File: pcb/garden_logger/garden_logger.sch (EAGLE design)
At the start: 2 parts

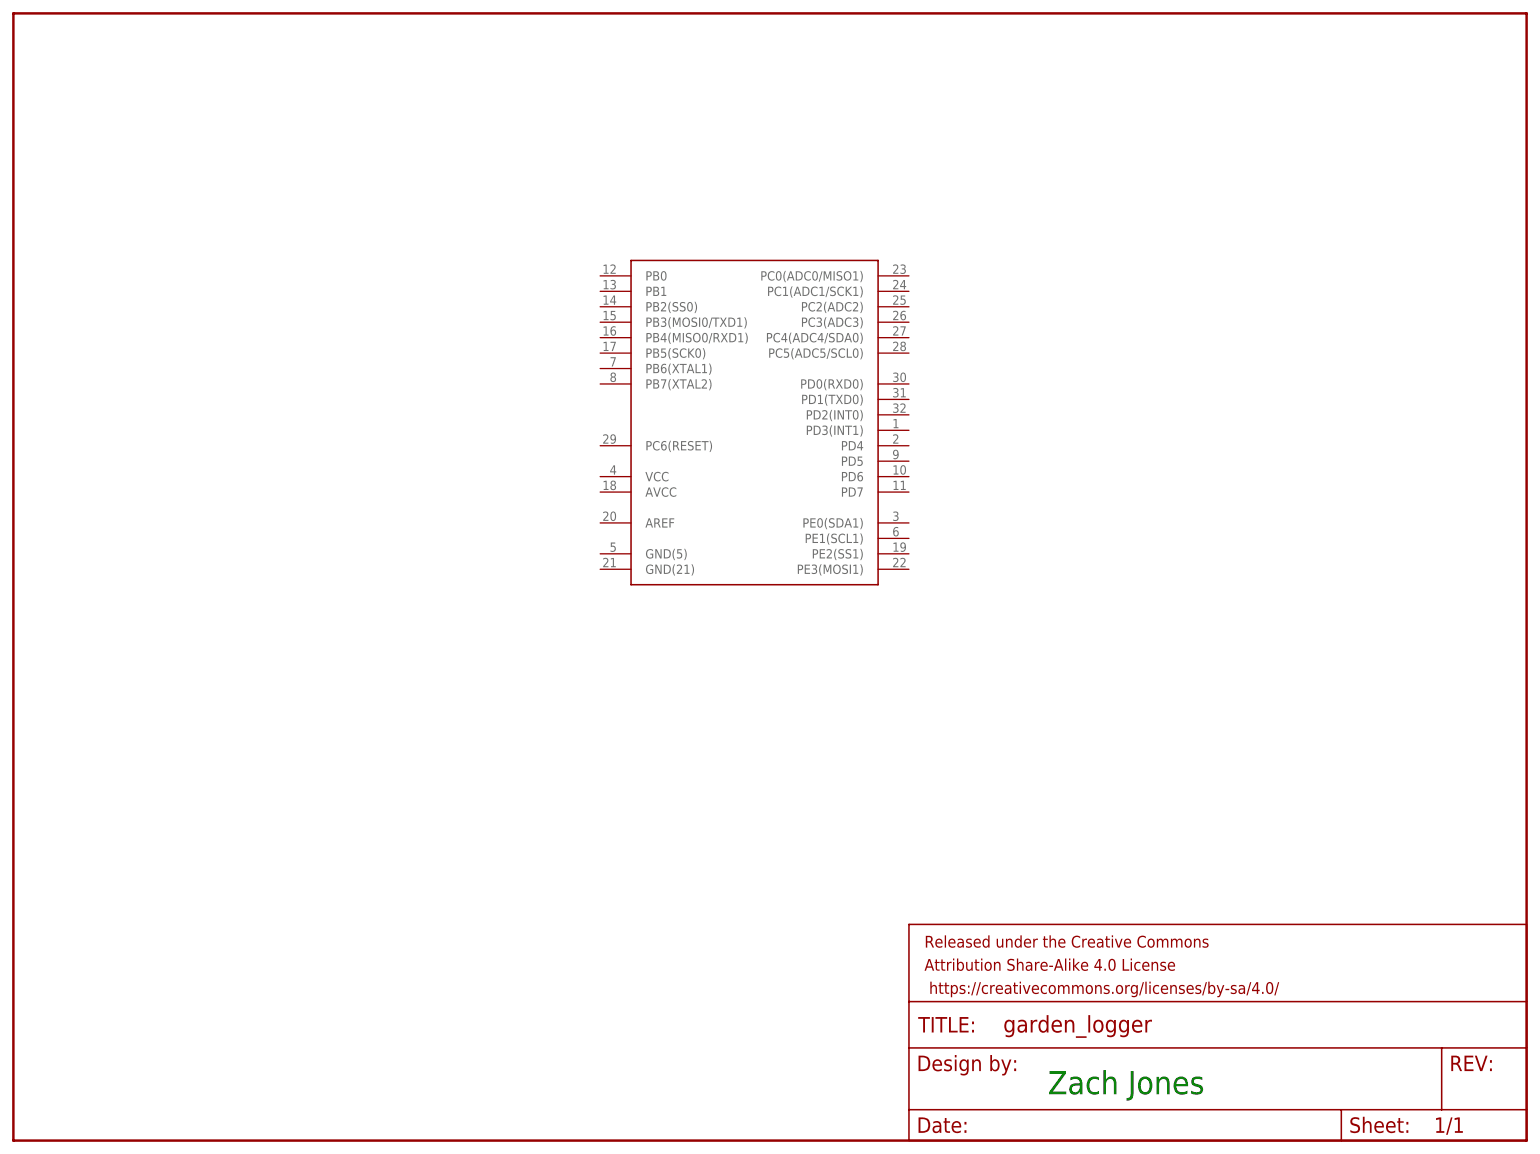
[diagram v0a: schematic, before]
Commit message: basic support circuit and breakout pin headers
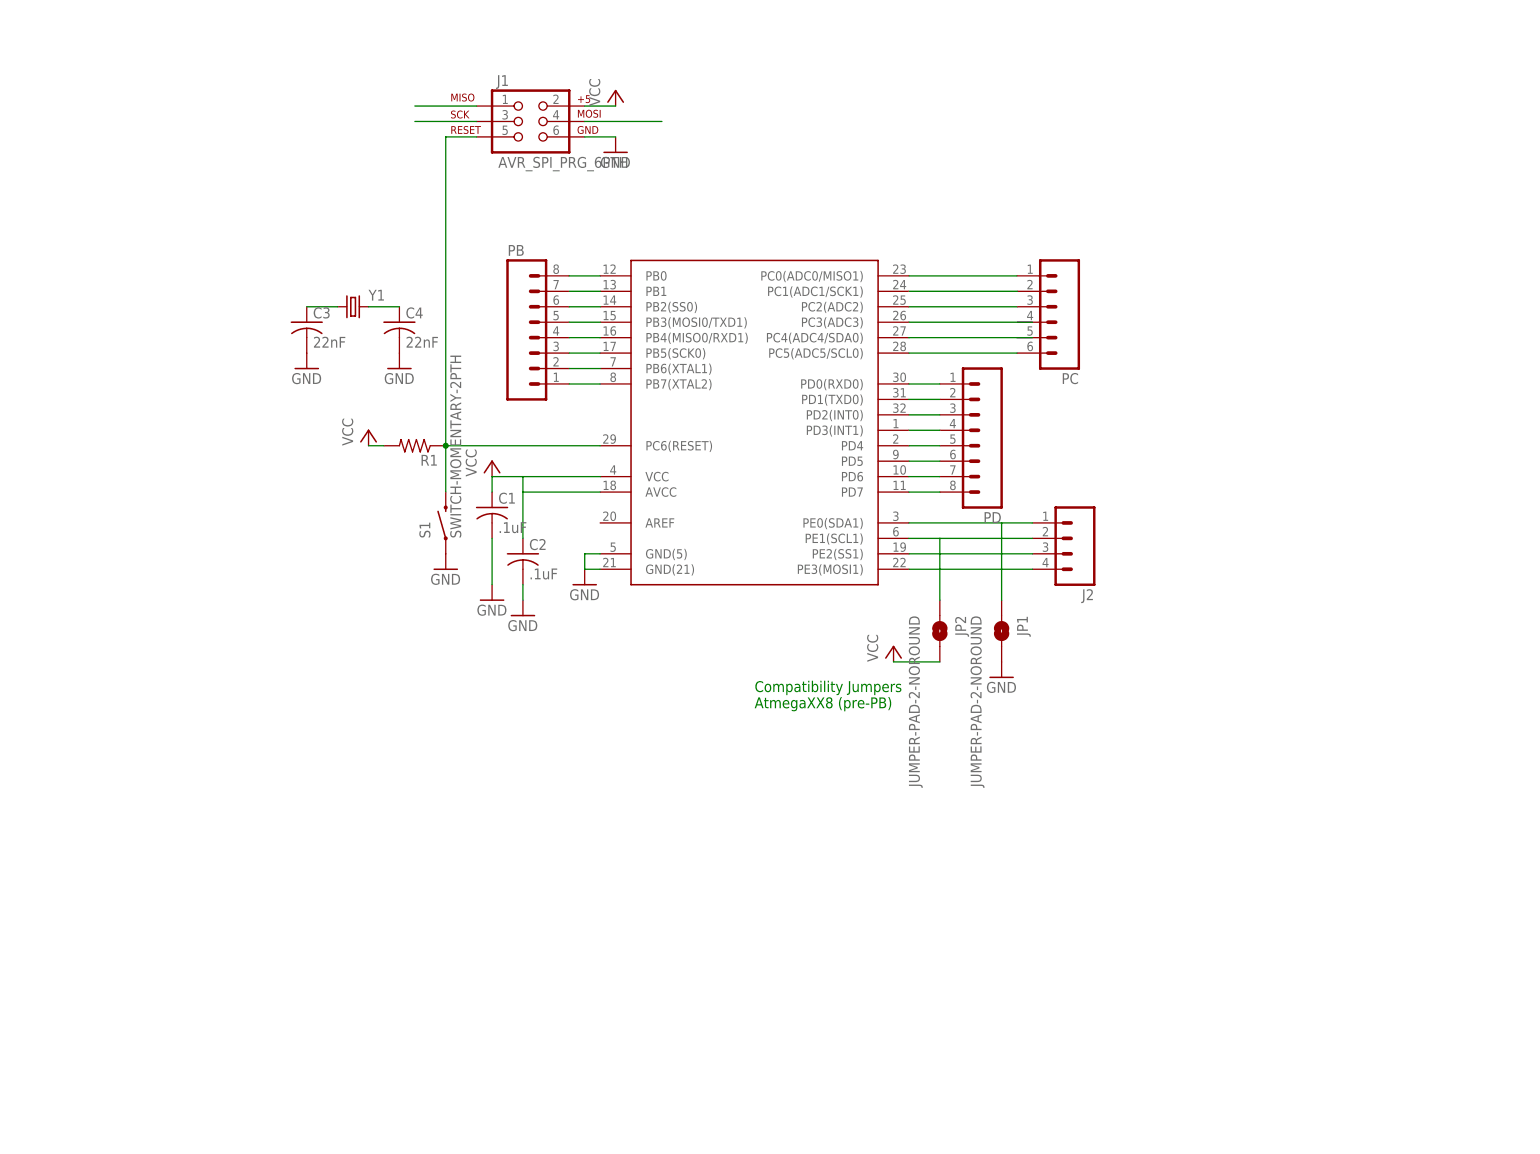
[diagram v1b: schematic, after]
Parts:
- removed FRAME1: FRAME-LETTER, SparkFun-Aesthetics:FRAME-LETTER
- added C1, C2: .1uF, rcl:C-USC0805
- added C3, C4: 22nF, rcl:C-USC0805
- added J1: AVR_SPI_PRG_6PTH, SparkFun-Connectors:AVR_SPI_PRG_6PTH
- added J2: (no value), SparkFun-Connectors:M04PTH
- added JP1, JP2: JUMPER-PAD-2-NOROUND, SparkFun-Passives:JUMPER-PAD-2-NOROUND
- added PB, PD: (no value), SparkFun-Connectors:M08
- added PC: (no value), SparkFun-Connectors:M06SILK_FEMALE_PTH
- added R1: (no value), rcl:R-US_R0805
- added S1: SWITCH-MOMENTARY-2PTH, SparkFun-Electromechanical:SWITCH-MOMENTARY-2PTH
- added Y1: (no value), SparkFun-FreqCtrl:CRYSTALHC49US
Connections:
- new net GND: C1.2, C2.2, C3.2, C4.2, J1.6, JP1.2, S1.1, U$1.GND(21), U$1.GND(5)
- new net N$1: J1.5, R1.1, S1.2, U$1.PC6(RESET)
- new net PIN1: PD.4, U$1.PD3(INT1)
- new net PIN10: PD.7, U$1.PD6
- new net PIN11: PD.8, U$1.PD7
- new net PIN12: PB.8, U$1.PB0
- new net PIN13: PB.7, U$1.PB1
- new net PIN14: PB.6, U$1.PB2(SS0)
- new net PIN15: J1.4, PB.5, U$1.PB3(MOSI0/TXD1)
- new net PIN16: J1.1, PB.4, U$1.PB4(MISO0/RXD1)
- new net PIN17: J1.3, PB.3, U$1.PB5(SCK0)
- new net PIN19: J2.3, U$1.PE2(SS1)
- new net PIN2: PD.5, U$1.PD4
- new net PIN22: J2.4, U$1.PE3(MOSI1)
- new net PIN23: PC.1, U$1.PC0(ADC0/MISO1)
- new net PIN24: PC.2, U$1.PC1(ADC1/SCK1)
- new net PIN25: PC.3, U$1.PC2(ADC2)
- new net PIN26: U$1.PC3(ADC3)
- new net PIN27: U$1.PC4(ADC4/SDA0)
- new net PIN28: PC.6, U$1.PC5(ADC5/SCL0)
- new net PIN3: J2.1, JP1.1, U$1.PE0(SDA1)
- new net PIN30: PD.1, U$1.PD0(RXD0)
- new net PIN31: PD.2, U$1.PD1(TXD0)
- new net PIN32: PD.3, U$1.PD2(INT0)
- new net PIN6: J2.2, JP2.1, U$1.PE1(SCL1)
- new net PIN7: C3.1, PB.2, U$1.PB6(XTAL1), Y1.1
- new net PIN8: C4.1, PB.1, U$1.PB7(XTAL2), Y1.2
- new net PIN9: PD.6, U$1.PD5
- new net VCC: C1.1, C2.1, J1.2, JP2.2, R1.2, U$1.AVCC, U$1.VCC
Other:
- note added: "Compatibility Jumpers AtmegaXX8 (pre-PB)"
- note removed: "Zach Jones"

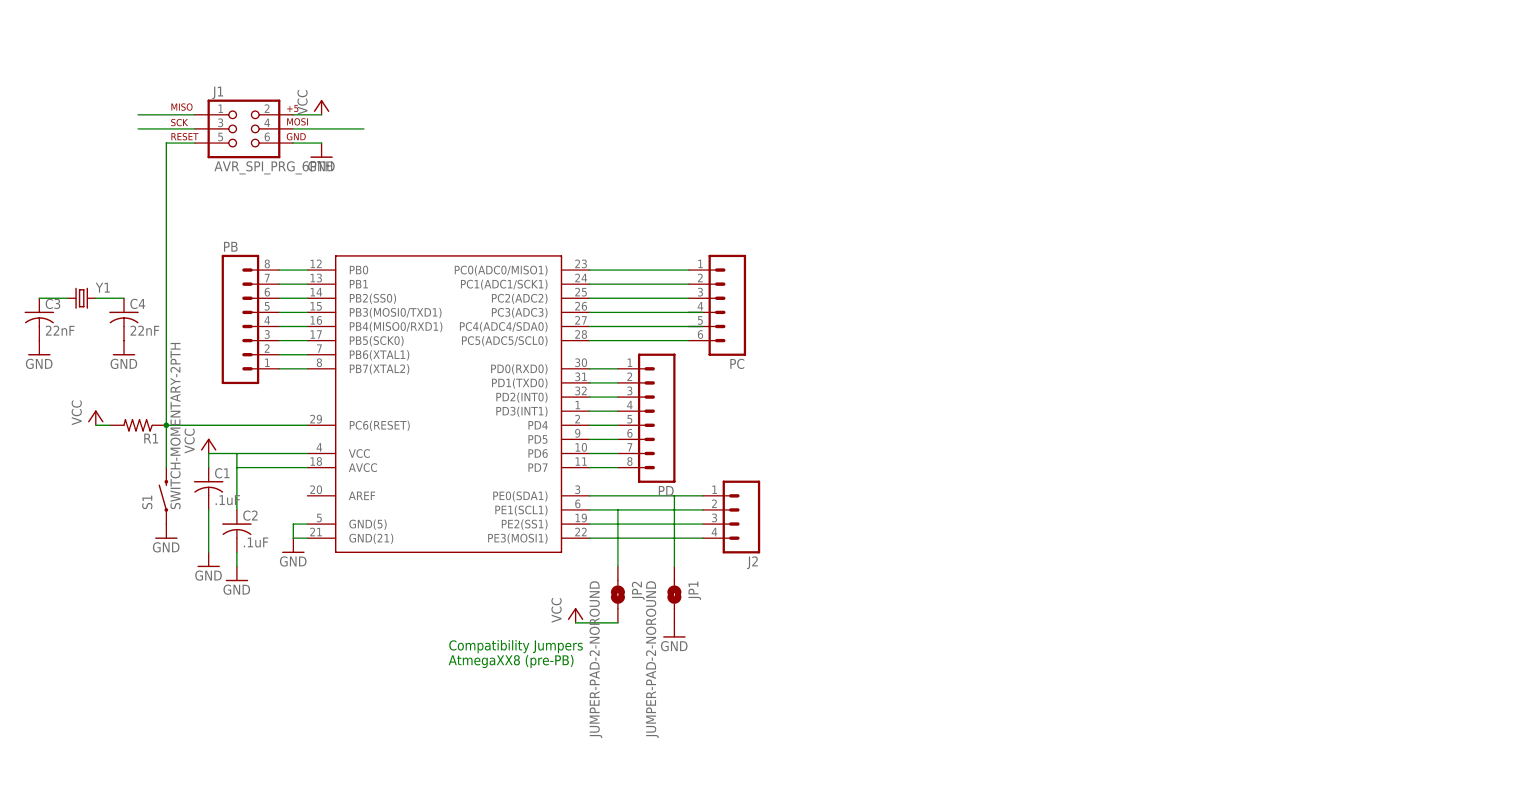
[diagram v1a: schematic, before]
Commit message: added some extra breakouts
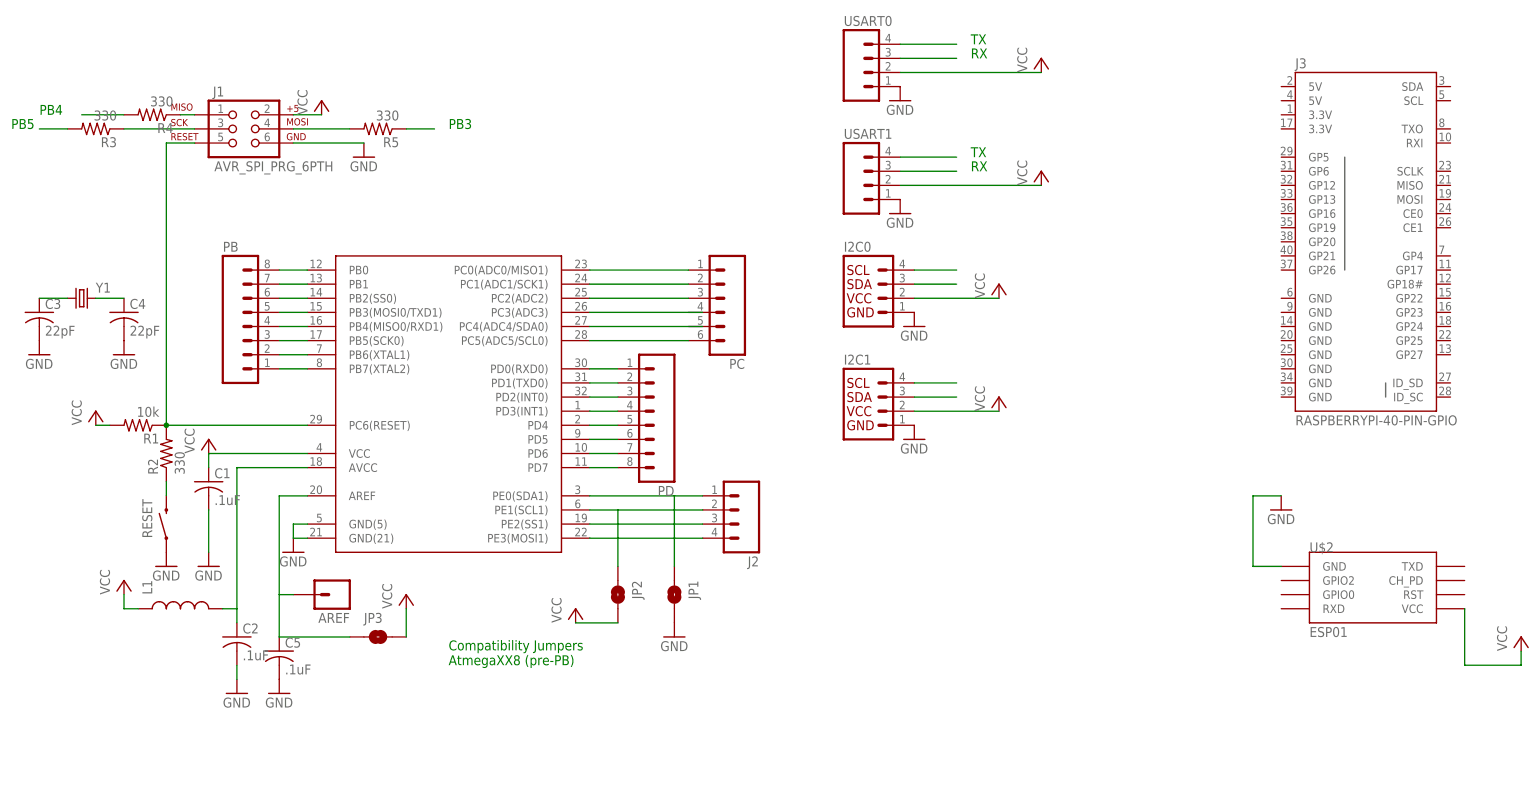
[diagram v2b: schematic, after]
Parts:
- removed S1: SWITCH-MOMENTARY-2PTH, SparkFun-Electromechanical:SWITCH-MOMENTARY-2PTH
- added AREF: (no value), SparkFun-Connectors:M01PTH
- added C5: .1uF, rcl:C-USC0805
- added I2C0, I2C1: (no value), SparkFun-Connectors:I2C_STANDARD
- added J3: RASPBERRYPI-40-PIN-GPIO, SparkFun-Boards:RASPBERRYPI-40-PIN-GPIO
- added JP3: JUMPER-PAD-2-NOROUND, SparkFun-Passives:JUMPER-PAD-2-NOROUND
- added L1: (no value), SparkFun-Passives:INDUCTOR0805
- added R2, R3, R4, R5: 330, rcl:R-US_R0805
- added RESET: SWITCH-MOMENTARY-2PTH, SparkFun-Electromechanical:SWITCH-MOMENTARY-2PTH
- added U$2: ESP01, esp8266modules:ESP01
- added USART0, USART1: (no value), SparkFun-Connectors:M04PTH
- C3, C4: value 22nF -> 22pF
- R1: value (none) -> 10k
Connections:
- net PIN1 renamed PD3
- net PIN10 renamed PD6
- net PIN11 renamed PD7
- net PIN12 renamed PB0
- net PIN13 renamed PB1
- net PIN14 renamed PB2
- net PIN19 renamed PE2
- net PIN2 renamed PD4
- net PIN22 renamed PE3
- net PIN23 renamed PC0
- net PIN24 renamed PC1
- net PIN25 renamed PC2
- net PIN26 renamed PC3
- net PIN32 renamed PD2
- net PIN7 renamed PB6
- net PIN8 renamed PB7
- net PIN9 renamed PD5
- removed net PIN15: J1.4, PB.5, U$1.PB3(MOSI0/TXD1)
- removed net PIN16: J1.1, PB.4, U$1.PB4(MISO0/RXD1)
- removed net PIN17: J1.3, PB.3, U$1.PB5(SCK0)
- removed net PIN27: U$1.PC4(ADC4/SDA0)
- removed net PIN28: PC.6, U$1.PC5(ADC5/SCL0)
- removed net PIN3: J2.1, JP1.1, U$1.PE0(SDA1)
- removed net PIN30: PD.1, U$1.PD0(RXD0)
- removed net PIN31: PD.2, U$1.PD1(TXD0)
- removed net PIN6: J2.2, JP2.1, U$1.PE1(SCL1)
- new net AVCC: C2.1, L1.2, U$1.AVCC
- new net N$2: R2.1, RESET.2
- new net N$3: J1.1, R4.1
- new net N$4: J1.3, R3.1
- new net N$5: J1.4, R5.2
- new net PB3: PB.5, R5.1, U$1.PB3(MOSI0/TXD1), USART1.3, USART1.4
- new net PB4: PB.4, R4.2, U$1.PB4(MISO0/RXD1)
- new net PB5: PB.3, R3.2, U$1.PB5(SCK0)
- new net PC4: I2C0.3, U$1.PC4(ADC4/SDA0)
- new net PC5: I2C0.4, PC.6, U$1.PC5(ADC5/SCL0)
- new net PC6: J1.5, R1.1, R2.2, U$1.PC6(RESET)
- new net PD0: PD.1, U$1.PD0(RXD0), USART0.3
- new net PD1: PD.2, U$1.PD1(TXD0), USART0.4
- new net PE0: I2C1.3, J2.1, JP1.1, U$1.PE0(SDA1)
- new net PE1: I2C1.4, J2.2, JP2.1, U$1.PE1(SCL1)
- net GND: now also C5.2, I2C0.1, I2C1.1, RESET.1, U$2.GND, USART0.1, USART1.1; no longer S1.1
- net N$1: now also AREF.1, C5.1, JP3.1, U$1.AREF; no longer J1.5, R1.1, S1.2, U$1.PC6(RESET)
- net VCC: now also I2C0.2, I2C1.2, JP3.2, L1.1, U$2.VCC, USART0.2, USART1.2; no longer C2.1, U$1.AVCC
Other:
- note added: "PB3"
- note added: "PB4"
- note added: "PB5"
- note added: "RX"
- note added: "TX"
- moved on the sheet: C2

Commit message: most avr stuff connected.  working on rpi breakout section.  added emtpy board layout
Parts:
- added H1, H2, H3, H4: STAND-OFF, SparkFun-Electromechanical:STAND-OFF
- added J4: (no value), SparkFun-Connectors:M02PTH
- added JP4, JP5: JUMPER-PAD-2-NOROUND, SparkFun-Passives:JUMPER-PAD-2-NOROUND
- added L2: 10uH, SparkFun-Passives:INDUCTOR0805
- added LOGO1: OSHW-LOGOS, SparkFun-Aesthetics:OSHW-LOGOS
- added RPI-I2C: (no value), SparkFun-Connectors:I2C_STANDARD
- added RPI-USART: (no value), SparkFun-Connectors:M04PTH
- L1: value (none) -> 10uH
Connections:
- new net AVRVCC: C1.1, L2.2, U$1.VCC
- new net N$12: J3.SCL, RPI-I2C.4
- new net N$13: J3.SDA, RPI-I2C.3
- new net N$6: J4.1, JP5.2, U$2.CH_PD
- new net N$7: J4.2, JP4.1, U$2.RST
- new net N$8: J3.TXO, RPI-USART.4
- new net N$9: J3.RXI, RPI-USART.3
- net GND: now also J3.GND@14, J3.GND@20, J3.GND@25, J3.GND@30, J3.GND@34, J3.GND@39, J3.GND@6, J3.GND@9, RPI-I2C.1, RPI-USART.1
- net PD0: now also U$2.TXD
- net PD1: now also U$2.RXD
- net PD6: now also JP5.1
- net PD7: now also JP4.2
- net VCC: now also L2.1, RPI-I2C.2, RPI-USART.2; no longer C1.1, U$1.VCC
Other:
- note added: "Jumpering over inductor pads if not including inductors"
- note added: "PD0"
- note added: "PD1"
- moved on the sheet: C1, C2, L1, RESET

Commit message: added buttons and leds.  started laying out board
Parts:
- added ADC: (no value), SparkFun-Connectors:M08
- added BUTTON, LED: (no value), SparkFun-Connectors:M03PTH
- added BUTTON1, BUTTON2, BUTTON3: SWITCH-MOMENTARY-2PTH, SparkFun-Electromechanical:SWITCH-MOMENTARY-2PTH
- added LED1, LED2, LED3: (no value), led:LEDCHIPLED_0805
- added R10, R11, R9: 10k, rcl:R-US_R0805
- added R6, R7, R8: 330, rcl:R-US_R0805
- renumbered J2 to PE, J4 to ESP-01
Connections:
- new net N$11: LED1.C, R6.2
- new net N$14: LED2.C, R7.2
- new net N$15: LED3.C, R8.2
- new net N$16: LED.1, LED1.A
- new net N$17: LED.2, LED2.A
- new net N$18: LED.3, LED3.A
- new net N$20: BUTTON.3, BUTTON3.2, R11.2
- new net N$21: BUTTON.2, BUTTON2.2, R10.2
- new net N$22: BUTTON.1, BUTTON1.2, R9.2
- net GND: now also BUTTON1.1, BUTTON2.1, BUTTON3.1, R6.1, R7.1, R8.1
- net PC0: now also ADC.1
- net PC1: now also ADC.2
- net PC2: now also ADC.3
- net PC3: now also ADC.4
- net PC4: now also ADC.5
- net PC5: now also ADC.6
- net PE2: now also ADC.7
- net PE3: now also ADC.8
- net VCC: now also R10.1, R11.1, R9.1

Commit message: removed rpi header to have bigger proto area.  Mostly done routeing
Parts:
- removed ADC: (no value), SparkFun-Connectors:M08
- removed ESP-01: (no value), SparkFun-Connectors:M02PTH
- removed J3: RASPBERRYPI-40-PIN-GPIO, SparkFun-Boards:RASPBERRYPI-40-PIN-GPIO
- removed JP1, JP2, JP3, JP4, JP5: JUMPER-PAD-2-NOROUND, SparkFun-Passives:JUMPER-PAD-2-NOROUND
- removed RPI-I2C: (no value), SparkFun-Connectors:I2C_STANDARD
- removed RPI-USART: (no value), SparkFun-Connectors:M04PTH
- added C10, C6: 100uF, SparkFun-Passives:CAP_POLPTH1
- added C7: .1uF, rcl:C-USC0805
- added C8, C9: 1uF, rcl:C-USC0805
- added COMPAT1, COMPAT2: SOLDERJUMPER-OLDNO, SparkFun-Retired:SOLDERJUMPER-OLDNO
- added ESP01: (no value), SparkFun-Connectors:M04PTH
- added F1: PTCSMD, SparkFun-PowerIC:PTCSMD
- added GND, PROTO0, PROTO1, PROTO10, PROTO11, PROTO12, PROTO13, PROTO14, PROTO2, PROTO3, PROTO4, PROTO5, PROTO6, PROTO7, PROTO8, PROTO9, VCC: (no value), SparkFun-Connectors:M08
- added J2: POWER_JACKPTH, SparkFun-Connectors:POWER_JACKPTH
- added L3: 10uH, SparkFun-Passives:INDUCTOR0805
- added POWER: (no value), SparkFun-Connectors:M02PTH
- added PWR_LED: (no value), led:LEDCHIPLED_0805
- added R12: 330, rcl:R-US_R0805
- added U$3: MCP1702, zjembedded_eagle:MCP1702
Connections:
- new net N$10: F1.1, J2.PWR, POWER.1
- new net N$19: C9.1, L3.1, U$3.VOUT
- net GND: now also C10.-, C6.-, C7.2, C8.2, C9.2, COMPAT1.2, GND.1, GND.2, GND.3, GND.4, GND.5, GND.6, GND.7, GND.8, J2.GND, J2.GNDBREAK, POWER.2, R12.1, U$3.GND; no longer J3.GND@14, J3.GND@20, J3.GND@25, J3.GND@30, J3.GND@34, J3.GND@39, J3.GND@6, J3.GND@9, JP1.2, RPI-I2C.1, RPI-USART.1
- net N$1: no longer JP3.1
- net N$12: now also ESP01.3, U$2.RST; no longer J3.SCL, RPI-I2C.4
- net N$13: now also ESP01.4, U$2.RXD; no longer J3.SDA, RPI-I2C.3
- net N$6: now also ESP01.1, U$2.TXD; no longer ESP-01.1, JP5.2, U$2.CH_PD
- net N$7: now also ESP01.2, U$2.CH_PD; no longer ESP-01.2, JP4.1, U$2.RST
- net N$8: now also C8.1, F1.2, U$3.VIN; no longer J3.TXO, RPI-USART.4
- net N$9: now also PWR_LED.C, R12.2; no longer J3.RXI, RPI-USART.3
- net PB3: no longer USART1.3
- net PB4: now also USART1.3
- net PC0: no longer ADC.1
- net PC1: no longer ADC.2
- net PC2: no longer ADC.3
- net PC3: now also PC.4; no longer ADC.4
- net PC4: now also PC.5; no longer ADC.5
- net PC5: no longer ADC.6
- net PD0: no longer U$2.TXD
- net PD1: no longer U$2.RXD
- net PD6: no longer JP5.1
- net PD7: no longer JP4.2
- net PE0: now also COMPAT1.1; no longer JP1.1
- net PE1: now also COMPAT2.1; no longer JP2.1
- net PE2: no longer ADC.7
- net PE3: no longer ADC.8
- net VCC: now also C10.+, C6.+, C7.1, COMPAT2.2, L3.2, PWR_LED.A, VCC.1, VCC.2, VCC.3, VCC.4, VCC.5, VCC.6, VCC.7, VCC.8; no longer JP2.2, JP3.2, RPI-I2C.2, RPI-USART.2
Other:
- note removed: "PD0"
- note removed: "PD1"
- moved on the sheet: PB, PC, PD, PE
